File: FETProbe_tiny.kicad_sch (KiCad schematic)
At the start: 17 parts, among them J1 u.Fl, J5 u.Fl, Q1 BF998

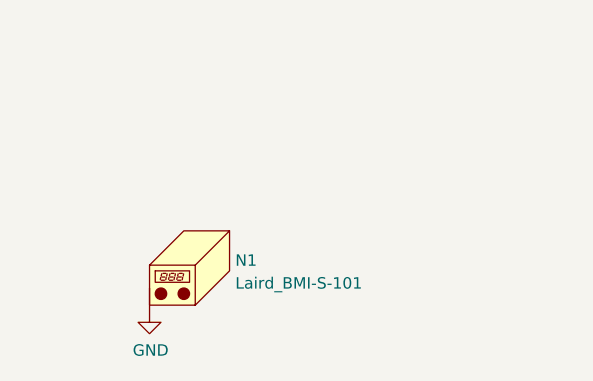
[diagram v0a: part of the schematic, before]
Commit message: Add additional shield vendor
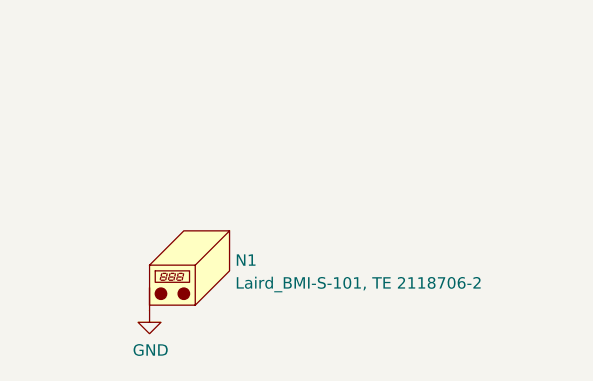
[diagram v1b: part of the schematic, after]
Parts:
- N1: value Laird_BMI-S-101 -> Laird_BMI-S-101, TE 2118706-2
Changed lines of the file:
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@@
       (effects (font (size 1.27 1.27)) (justify left))
     )
-    (property "Value" "Laird_BMI-S-101" (id 1) (at 229.235 144.2597 0)
+    (property "Value" "Laird_BMI-S-101, TE 2118706-2" (id 1) (at 229.235 144.2597 0)
       (effects (font (size 1.27 1.27)) (justify left))
     )
@@
     )
     (path "/a543a4a0-b8e2-45a4-be48-7207020a5b1f"
-      (reference "N1") (unit 1) (value "Laird_BMI-S-101") (footprint "RF_Shielding:Laird_Technologies_BMI-S-101_13.66x12.70mm")
+      (reference "N1") (unit 1) (value "Laird_BMI-S-101, TE 2118706-2") (footprint "RF_Shielding:Laird_Technologies_BMI-S-101_13.66x12.70mm")
     )
     (path "/31bfc3e7-147b-4531-a0c5-e3a305c1647d"
